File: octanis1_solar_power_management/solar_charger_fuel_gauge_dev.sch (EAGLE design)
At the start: 66 parts, among them IC1 REG1117, Q1 32.768kHz, T1 BC547, T2 BC547, U1 BQ24210, U2 BQ27510_DRZ_12, U3 DRV8836DSSR, U4 DRV8836DSSR, U5 DRV8836DSSR, U6 MSP430F5529IPNR, U7 DRV8836DSSR

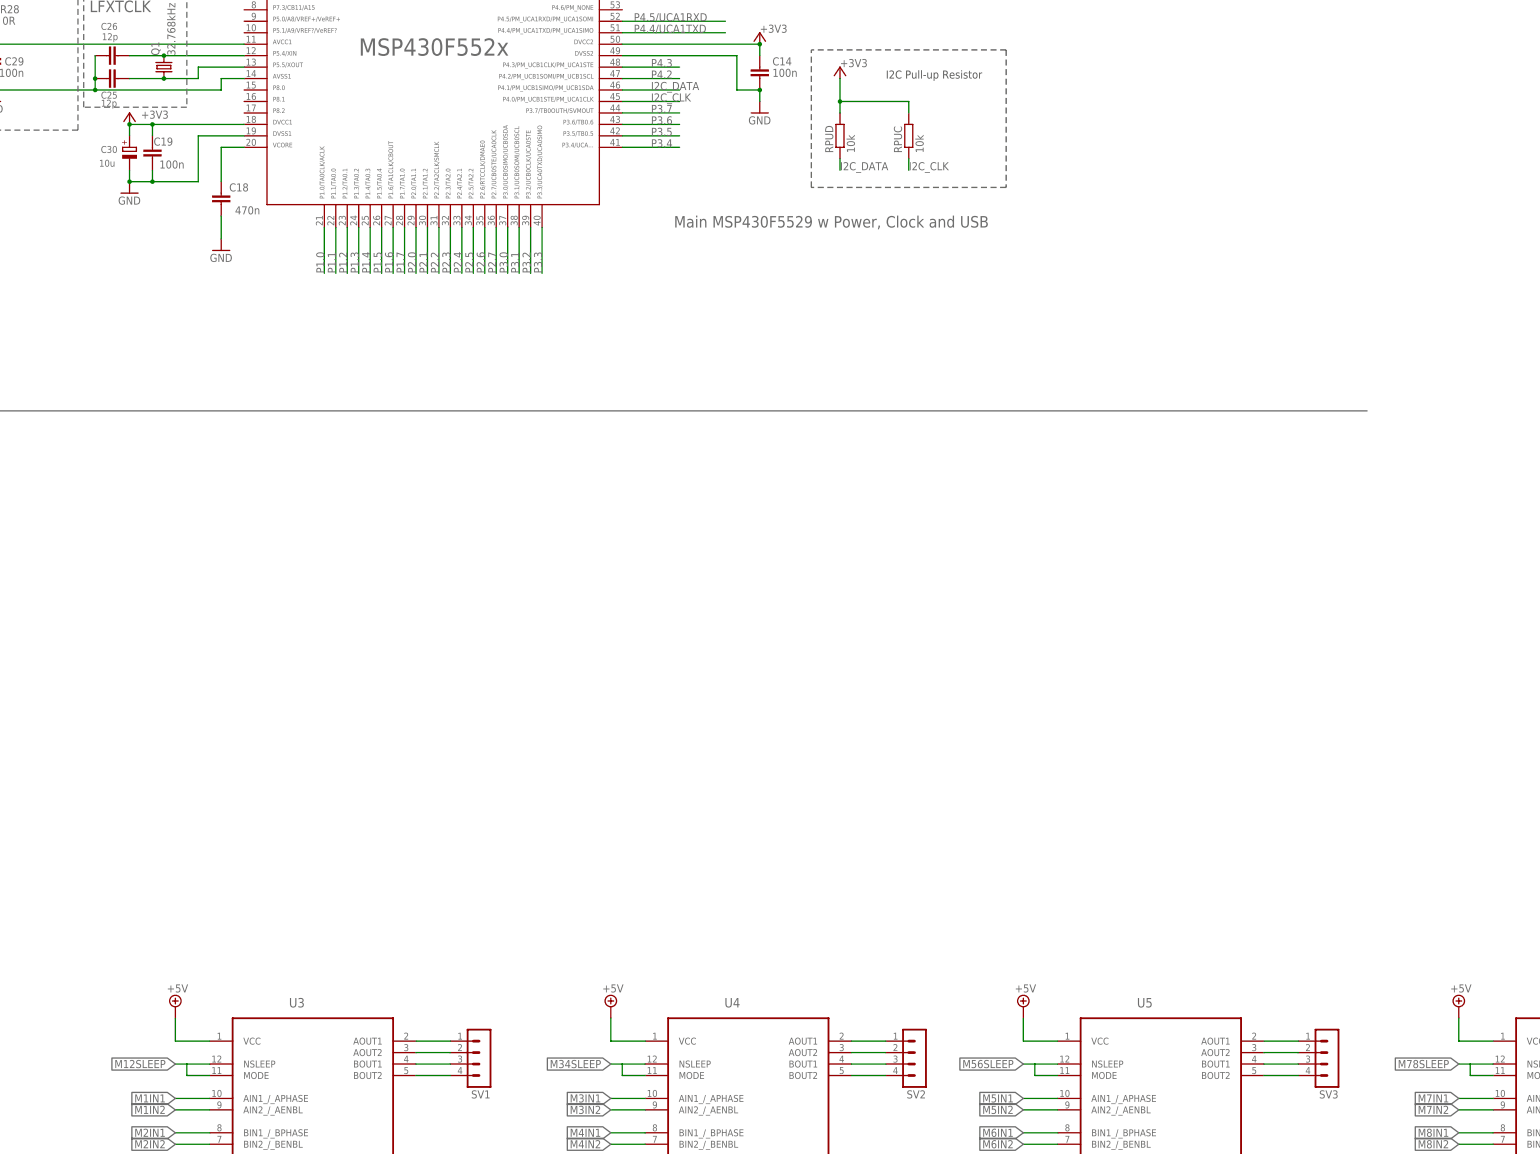
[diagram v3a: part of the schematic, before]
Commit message: mapped ports for motors
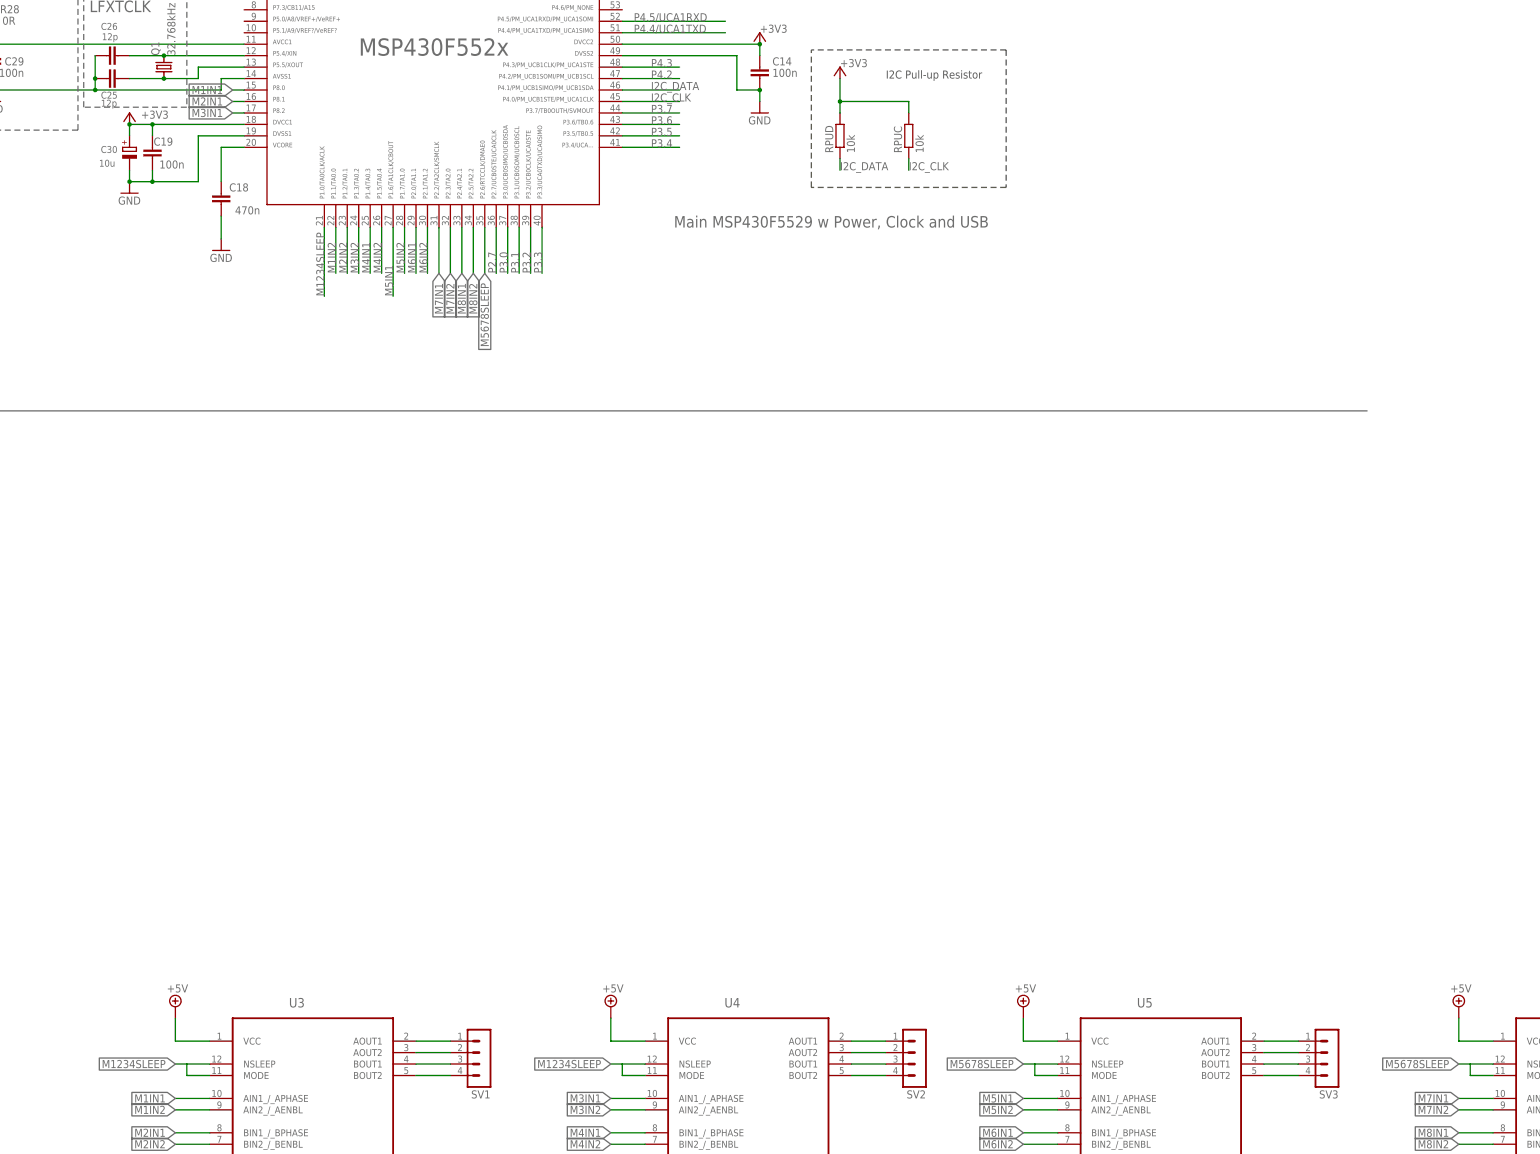
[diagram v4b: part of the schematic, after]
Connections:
- removed net M12SLEEP: U3.MODE, U3.NSLEEP
- removed net M34SLEEP: U4.MODE, U4.NSLEEP
- removed net M56SLEEP: U5.MODE, U5.NSLEEP
- removed net M78SLEEP: U7.MODE, U7.NSLEEP
- removed net P1.0: U6.21
- removed net P1.1: U6.22
- removed net P1.2: U6.23
- removed net P1.3: U6.24
- removed net P1.4: U6.25
- removed net P1.5: U6.26
- removed net P1.6: U6.27
- removed net P1.7: U6.28
- removed net P2.0: U6.29
- removed net P2.1: U6.30
- removed net P2.2: U6.31
- removed net P2.3: U6.32
- removed net P2.4: U6.33
- removed net P2.5: U6.34
- removed net P2.6: U6.35
- new net M1234SLEEP: U3.MODE, U3.NSLEEP, U4.MODE, U4.NSLEEP, U6.21
- new net M5678SLEEP: U5.MODE, U5.NSLEEP, U6.35, U7.MODE, U7.NSLEEP
- net M1IN1: now also U6.15
- net M1IN2: now also U6.22
- net M2IN1: now also U6.16
- net M2IN2: now also U6.23
- net M3IN1: now also U6.17
- net M3IN2: now also U6.24
- net M4IN1: now also U6.25
- net M4IN2: now also U6.26
- net M5IN1: now also U6.27
- net M5IN2: now also U6.28
- net M6IN1: now also U6.29
- net M6IN2: now also U6.30
- net M7IN1: now also U6.31
- net M7IN2: now also U6.32
- net M8IN1: now also U6.33
- net M8IN2: now also U6.34

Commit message: added gyro, accelerometer, pressure sensor, compass, serial connectors, analog input pins.
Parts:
- added ANALOG: (no value), pinhead:PINHD-1X6
- added C10: 4.7µ, rcl:C-EUC0603
- added C11: 0.1uF, rcl:C-EUC0603
- added C12: 10uF, resistor:CPOL-EUA/3216-18R
- added C13: 0.22µ, rcl:C-EUC0603
- added C15: 0.1µ, rcl:C-EUC0603
- added C16, C20: 100nF, rcl:C-EUC0603
- added C17: 10nF, rcl:C-EUC0603
- added C21: 2,2nF, rcl:C-EUC0603
- added COMPASS: HMC5883L, HMC5883L:HMC5883L
- added I2C: I2C, pinhead:PINHD-1X2
- added IC2: MPU-6050, seb:MPU-6050
- added JP2: (no value), pinhead:PINHD-1X4
- added U9: BMP180, SparkFun-Sensors:BMP180
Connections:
- removed net I2C_CLK: RPUC.1, U2.SCL, U6.45
- removed net I2C_DATA: RPUD.1, U2.SDA, U6.46
- removed net P4.2: U6.47
- removed net P4.3: U6.48
- removed net P4.4/UCA1TXD: U6.51
- removed net P4.5/UCA1RXD: U6.52
- removed net P7.0: U6.5
- new net N$17: C10.1, COMPASS.C1
- new net N$18: C16.2, IC2.10
- new net N$19: C21.1, IC2.20
- new net N$25: C13.2, COMPASS.SETP
- new net N$32: C13.1, COMPASS.SETC
- new net P5.0: ANALOG.2, U6.9
- new net P5.1: ANALOG.1, U6.10
- new net RX: JP2.3, U6.52
- new net SCL: COMPASS.SCL, I2C.1, IC2.23, RPUC.1, U2.SCL, U6.47, U9.SCL
- new net SDA: COMPASS.SDA, I2C.2, IC2.24, RPUD.1, U2.SDA, U6.46, U9.SDA
- new net SPI_CLK: JP2.1, U6.45
- new net SPI_SLAVE_EN: JP2.4, U6.48
- new net TX: JP2.2, U6.51
- net +3V3: now also C11.1, C12.+, C15.2, C17.2, C20.1, COMPASS.S1, COMPASS.VDD, COMPASS.VDD_IO, IC2.13, IC2.8, U9.VDD, U9.VDDIO
- net GND: now also C10.2, C11.2, C12.-, C15.1, C16.1, C17.1, C20.2, C21.2, COMPASS.GND, IC2.1, IC2.11, IC2.18, IC2.9, IC2.P, U9.GND
- net P6.4: now also ANALOG.6
- net P6.5: now also ANALOG.5
- net P6.6: now also ANALOG.4
- net P6.7: now also ANALOG.3
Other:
- note added: "Pressure Sensor"
- note added: "compass"
- moved on the sheet: SV1, SV2, SV3, SV4, U3, U4, U5, U7

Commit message: created gerber files, with logo. In v0.1
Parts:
- added DIGITAL1: (no value), pinhead:PINHD-1X6
- added DIGITAL2: (no value), pinhead:PINHD-1X8
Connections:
- new net N$14: DIGITAL2.1, U6.60
- new net N$15: DIGITAL2.2, U6.59
- new net N$20: DIGITAL2.3, U6.58
- new net N$21: DIGITAL2.4, U6.57
- new net N$22: DIGITAL2.5, U6.56
- new net N$23: DIGITAL2.6, U6.55
- new net N$24: DIGITAL2.7, U6.54
- new net N$26: DIGITAL2.8, U6.53
- net P2.7: now also DIGITAL1.6
- net P3.0: now also DIGITAL1.5
- net P3.1: now also DIGITAL1.4
- net P3.2: now also DIGITAL1.3
- net P3.3: now also DIGITAL1.2
- net P3.4: now also DIGITAL1.1
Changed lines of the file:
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@@
 <part name="JP2" library="pinhead" deviceset="PINHD-1X4" device=""/>
 <part name="ANALOG" library="pinhead" deviceset="PINHD-1X6" device=""/>
+<part name="DIGITAL1" library="pinhead" deviceset="PINHD-1X6" device=""/>
+<part name="DIGITAL2" library="pinhead" deviceset="PINHD-1X8" device=""/>
 </parts>
 <sheets>
@@
 <instance part="JP2" gate="A" x="434.34" y="167.64"/>
 <instance part="ANALOG" gate="A" x="281.94" y="261.62" rot="R180"/>
+<instance part="DIGITAL1" gate="A" x="391.16" y="157.48" rot="R270"/>
+<instance part="DIGITAL2" gate="A" x="416.56" y="241.3"/>
 </instances>
 <busses>
@@
 <net name="P3.2" class="0">
 <segment>
-<wire x1="375.92" y1="175.26" x2="375.92" y2="185.42" width="0.1524" layer="91"/>
+<wire x1="393.7" y1="160.02" x2="393.7" y2="172.72" width="0.1524" layer="91"/>
+<wire x1="393.7" y1="172.72" x2="375.92" y2="172.72" width="0.1524" layer="91"/>
+<wire x1="375.92" y1="172.72" x2="375.92" y2="185.42" width="0.1524" layer="91"/>
 <pinref part="U6" gate="G$1" pin="39"/>
 <label x="375.92" y="175.26" size="1.778" layer="95" rot="R90"/>
+<pinref part="DIGITAL1" gate="A" pin="3"/>
 </segment>
 </net>
@@
 <label x="402.59" y="203.2" size="1.778" layer="95"/>
 <wire x1="396.24" y1="203.2" x2="408.94" y2="203.2" width="0.1524" layer="91"/>
+<wire x1="408.94" y1="203.2" x2="408.94" y2="175.26" width="0.1524" layer="91"/>
+<wire x1="408.94" y1="175.26" x2="398.78" y2="175.26" width="0.1524" layer="91"/>
+<pinref part="DIGITAL1" gate="A" pin="1"/>
+<wire x1="398.78" y1="175.26" x2="398.78" y2="160.02" width="0.1524" layer="91"/>
 </segment>
 </net>
 <net name="P3.3" class="0">
 <segment>
+<wire x1="396.24" y1="160.02" x2="396.24" y2="175.26" width="0.1524" layer="91"/>
+<wire x1="396.24" y1="175.26" x2="378.46" y2="175.26" width="0.1524" layer="91"/>
 <wire x1="378.46" y1="175.26" x2="378.46" y2="185.42" width="0.1524" layer="91"/>
 <pinref part="U6" gate="G$1" pin="40"/>
 <label x="378.46" y="175.26" size="1.778" layer="95" rot="R90"/>
+<pinref part="DIGITAL1" gate="A" pin="2"/>
 </segment>
 </net>
 <net name="P2.7" class="0">
 <segment>
-<wire x1="368.3" y1="175.26" x2="368.3" y2="185.42" width="0.1524" layer="91"/>
+<wire x1="386.08" y1="160.02" x2="386.08" y2="165.1" width="0.1524" layer="91"/>
+<wire x1="386.08" y1="165.1" x2="368.3" y2="165.1" width="0.1524" layer="91"/>
+<wire x1="368.3" y1="165.1" x2="368.3" y2="185.42" width="0.1524" layer="91"/>
 <pinref part="U6" gate="G$1" pin="36"/>
 <label x="368.3" y="175.26" size="1.778" layer="95" rot="R90"/>
+<pinref part="DIGITAL1" gate="A" pin="6"/>
 </segment>
 </net>
@@
 <net name="P3.0" class="0">
 <segment>
-<wire x1="370.84" y1="175.26" x2="370.84" y2="185.42" width="0.1524" layer="91"/>
+<wire x1="388.62" y1="160.02" x2="388.62" y2="167.64" width="0.1524" layer="91"/>
+<wire x1="388.62" y1="167.64" x2="370.84" y2="167.64" width="0.1524" layer="91"/>
+<wire x1="370.84" y1="167.64" x2="370.84" y2="185.42" width="0.1524" layer="91"/>
 <pinref part="U6" gate="G$1" pin="37"/>
 <label x="370.84" y="175.26" size="1.778" layer="95" rot="R90"/>
+<pinref part="DIGITAL1" gate="A" pin="5"/>
 </segment>
 </net>
 <net name="P3.1" class="0">
 <segment>
-<wire x1="373.38" y1="175.26" x2="373.38" y2="185.42" width="0.1524" layer="91"/>
+<wire x1="391.16" y1="160.02" x2="391.16" y2="170.18" width="0.1524" layer="91"/>
+<wire x1="391.16" y1="170.18" x2="373.38" y2="170.18" width="0.1524" layer="91"/>
+<wire x1="373.38" y1="170.18" x2="373.38" y2="185.42" width="0.1524" layer="91"/>
 <pinref part="U6" gate="G$1" pin="38"/>
 <label x="373.38" y="175.26" size="1.778" layer="95" rot="R90"/>
+<pinref part="DIGITAL1" gate="A" pin="4"/>
 </segment>
 </net>
@@
 </segment>
 </net>
+<net name="N$14" class="0">
+<segment>
+<pinref part="U6" gate="G$1" pin="60"/>
+<pinref part="DIGITAL2" gate="A" pin="1"/>
+<wire x1="414.02" y1="251.46" x2="396.24" y2="251.46" width="0.1524" layer="91"/>
+</segment>
+</net>
+<net name="N$15" class="0">
+<segment>
+<pinref part="U6" gate="G$1" pin="59"/>
+<pinref part="DIGITAL2" gate="A" pin="2"/>
+<wire x1="414.02" y1="248.92" x2="396.24" y2="248.92" width="0.1524" layer="91"/>
+</segment>
+</net>
+<net name="N$20" class="0">
+<segment>
+<pinref part="U6" gate="G$1" pin="58"/>
+<pinref part="DIGITAL2" gate="A" pin="3"/>
+<wire x1="414.02" y1="246.38" x2="396.24" y2="246.38" width="0.1524" layer="91"/>
+</segment>
+</net>
+<net name="N$21" class="0">
+<segment>
+<pinref part="U6" gate="G$1" pin="57"/>
+<pinref part="DIGITAL2" gate="A" pin="4"/>
+<wire x1="414.02" y1="243.84" x2="396.24" y2="243.84" width="0.1524" layer="91"/>
+</segment>
+</net>
+<net name="N$22" class="0">
+<segment>
+<pinref part="U6" gate="G$1" pin="56"/>
+<pinref part="DIGITAL2" gate="A" pin="5"/>
+<wire x1="414.02" y1="241.3" x2="396.24" y2="241.3" width="0.1524" layer="91"/>
+</segment>
+</net>
+<net name="N$23" class="0">
+<segment>
+<pinref part="U6" gate="G$1" pin="55"/>
+<pinref part="DIGITAL2" gate="A" pin="6"/>
+<wire x1="414.02" y1="238.76" x2="396.24" y2="238.76" width="0.1524" layer="91"/>
+</segment>
+</net>
+<net name="N$24" class="0">
+<segment>
+<pinref part="U6" gate="G$1" pin="54"/>
+<pinref part="DIGITAL2" gate="A" pin="7"/>
+<wire x1="414.02" y1="236.22" x2="396.24" y2="236.22" width="0.1524" layer="91"/>
+</segment>
+</net>
+<net name="N$26" class="0">
+<segment>
+<pinref part="U6" gate="G$1" pin="53"/>
+<pinref part="DIGITAL2" gate="A" pin="8"/>
+<wire x1="414.02" y1="233.68" x2="396.24" y2="233.68" width="0.1524" layer="91"/>
+</segment>
+</net>
